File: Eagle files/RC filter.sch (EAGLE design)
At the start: 4 parts

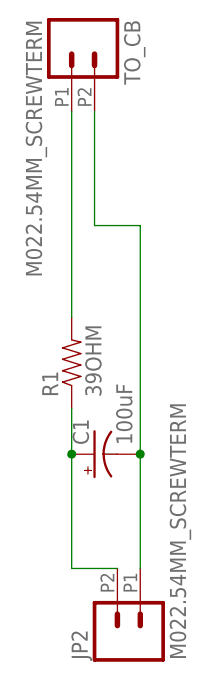
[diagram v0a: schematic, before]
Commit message: Changed screw terminal to 5.08 mm layout
Bumped board to v1.1
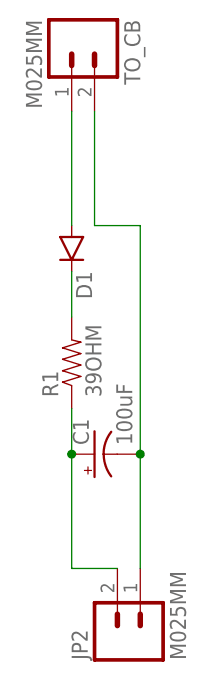
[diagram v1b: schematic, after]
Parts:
- added D1: (no value), SparkFun-DiscreteSemi:DIODESMA
- JP2, TO_CB: value M022.54MM_SCREWTERM -> M025MM; device SparkFun-Connectors:M022.54MM_SCREWTERM -> SparkFun-Connectors:M025MM
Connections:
- net N$2 renamed V_OUT
- new net V_IN: D1.A, TO_CB.1
- net N$1: now also D1.C; no longer TO_CB.1
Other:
- note added: "/Users/Stuart/Desktop/arrowtoy.bmp"
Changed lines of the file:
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@@
 <setting verticaltext="up"/>
 </settings>
-<grid distance="0.1" unitdist="inch" unit="inch" style="lines" multiple="1" display="no" altdistance="0.01" altunitdist="inch" altunit="inch"/>
+<grid distance="0.25" unitdist="mil" unit="mil" style="lines" multiple="1" display="yes" altdistance="0.01" altunitdist="inch" altunit="inch"/>
 <layers>
 <layer number="1" name="Top" color="4" fill="1" visible="no" active="no"/>
@@
 <layer number="132" name="bAdjust" color="7" fill="1" visible="yes" active="yes"/>
 <layer number="144" name="Drill_legend" color="7" fill="1" visible="no" active="yes"/>
-<layer number="150" name="Notes" color="7" fill="1" visible="yes" active="yes"/>
+<layer number="150" name="150bmp" color="1" fill="10" visible="yes" active="yes"/>
 <layer number="151" name="HeatSink" color="7" fill="1" visible="no" active="yes"/>
 <layer number="152" name="_bDocu" color="7" fill="1" visible="yes" active="yes"/>
@@
 <part name="C1" library="SparkFun-Capacitors" deviceset="100UF-10V-10%(TANT)" device="" value="100uF"/>
 <part name="R1" library="SparkFun-Resistors" deviceset="33OHM1/10W1%(0603)" device="" value="39OHM"/>
-<part name="TO_CB" library="SparkFun-Connectors" deviceset="M02" device="2.54MM_SCREWTERM"/>
-<part name="JP2" library="SparkFun-Connectors" deviceset="M02" device="2.54MM_SCREWTERM"/>
+<part name="TO_CB" library="SparkFun-Connectors" deviceset="M02" device="5MM" value="M025MM"/>
+<part name="JP2" library="SparkFun-Connectors" deviceset="M02" device="5MM" value="M025MM"/>
+<part name="D1" library="SparkFun-DiscreteSemi" deviceset="DIODE" device="SMA"/>
 </parts>
 <sheets>
 <sheet>
 <plain>
+<rectangle x1="0.028575" y1="5.108575" x2="0.034925" y2="5.114925" layer="150"/>
+<rectangle x1="5.692775" y1="5.121275" x2="5.699125" y2="5.127625" layer="150"/>
+<rectangle x1="0.466725" y1="5.610225" x2="0.473075" y2="5.616575" layer="150"/>
+<rectangle x1="5.254625" y1="5.622925" x2="5.260975" y2="5.629275" layer="150"/>
+<rectangle x1="0.511175" y1="5.661025" x2="0.517525" y2="5.667375" layer="150"/>
+<rectangle x1="5.210175" y1="5.673725" x2="5.216525" y2="5.680075" layer="150"/>
+<rectangle x1="5.165725" y1="5.724525" x2="5.172075" y2="5.730875" layer="150"/>
+<rectangle x1="0.777875" y1="5.965825" x2="0.784225" y2="5.972175" layer="150"/>
+<rectangle x1="0.949325" y1="6.162675" x2="0.955675" y2="6.169025" layer="150"/>
+<rectangle x1="0.993775" y1="6.213475" x2="1.000125" y2="6.219825" layer="150"/>
+<rectangle x1="4.594225" y1="6.378575" x2="4.600575" y2="6.384925" layer="150"/>
+<rectangle x1="1.343025" y1="6.613525" x2="1.349375" y2="6.619875" layer="150"/>
+<rectangle x1="1.431925" y1="6.715125" x2="1.438275" y2="6.721475" layer="150"/>
+<rectangle x1="4.289425" y1="6.727825" x2="4.295775" y2="6.734175" layer="150"/>
+<rectangle x1="1.476375" y1="6.765925" x2="1.482725" y2="6.772275" layer="150"/>
+<rectangle x1="4.244975" y1="6.778625" x2="4.251325" y2="6.784975" layer="150"/>
+<rectangle x1="1.520825" y1="6.816725" x2="1.527175" y2="6.823075" layer="150"/>
+<rectangle x1="4.111625" y1="6.931025" x2="4.117975" y2="6.937375" layer="150"/>
+<rectangle x1="1.914525" y1="7.267575" x2="1.920875" y2="7.273925" layer="150"/>
+<rectangle x1="3.806825" y1="7.280275" x2="3.813175" y2="7.286625" layer="150"/>
+<rectangle x1="1.958975" y1="7.318375" x2="1.965325" y2="7.324725" layer="150"/>
+<rectangle x1="3.762375" y1="7.331075" x2="3.768725" y2="7.337425" layer="150"/>
+<rectangle x1="3.717925" y1="7.369175" x2="3.724275" y2="7.375525" layer="150"/>
+<rectangle x1="3.717925" y1="7.381875" x2="3.724275" y2="7.388225" layer="150"/>
+<rectangle x1="2.047875" y1="7.419975" x2="2.054225" y2="7.426325" layer="150"/>
+<rectangle x1="3.368675" y1="7.781925" x2="3.375025" y2="7.788275" layer="150"/>
+<rectangle x1="2.441575" y1="7.870825" x2="2.447925" y2="7.877175" layer="150"/>
+<rectangle x1="3.279775" y1="7.883525" x2="3.286125" y2="7.889875" layer="150"/>
+<rectangle x1="2.486025" y1="7.921625" x2="2.492375" y2="7.927975" layer="150"/>
+<rectangle x1="3.235325" y1="7.934325" x2="3.241675" y2="7.940675" layer="150"/>
+<rectangle x1="2.549525" y1="7.985125" x2="2.555875" y2="7.991475" layer="150"/>
+<text x="0" y="-0.03175" size="0.0127" layer="150" font="vector">/Users/Stuart/Desktop/arrowtoy.bmp</text>
 </plain>
 <instances>
@@
 <instance part="TO_CB" gate="G$1" x="83.82" y="76.2" rot="R270"/>
 <instance part="JP2" gate="G$1" x="91.44" y="10.16" rot="R90"/>
+<instance part="D1" gate="G$1" x="83.82" y="53.34" rot="R270"/>
 </instances>
 <busses>
 </busses>
 <nets>
-<net name="N$1" class="0">
-<segment>
-<pinref part="R1" gate="G$1" pin="2"/>
+<net name="V_IN" class="0">
+<segment>
 <pinref part="TO_CB" gate="G$1" pin="1"/>
-<wire x1="83.82" y1="45.72" x2="83.82" y2="68.58" width="0.1524" layer="91"/>
-</segment>
-</net>
-<net name="N$2" class="0">
+<pinref part="D1" gate="G$1" pin="A"/>
+<wire x1="83.82" y1="55.88" x2="83.82" y2="68.58" width="0.1524" layer="91"/>
+</segment>
+</net>
+<net name="V_OUT" class="0">
 <segment>
 <pinref part="C1" gate="G$1" pin="+"/>
@@
 </segment>
 </net>
+<net name="N$1" class="0">
+<segment>
+<pinref part="D1" gate="G$1" pin="C"/>
+<pinref part="R1" gate="G$1" pin="2"/>
+<wire x1="83.82" y1="45.72" x2="83.82" y2="50.8" width="0.1524" layer="91"/>
+</segment>
+</net>
